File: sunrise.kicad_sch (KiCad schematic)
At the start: 18 parts, among them J1 TOP_HDR, J2 BTM_HDR, U1 LM3410, U2 LP5012

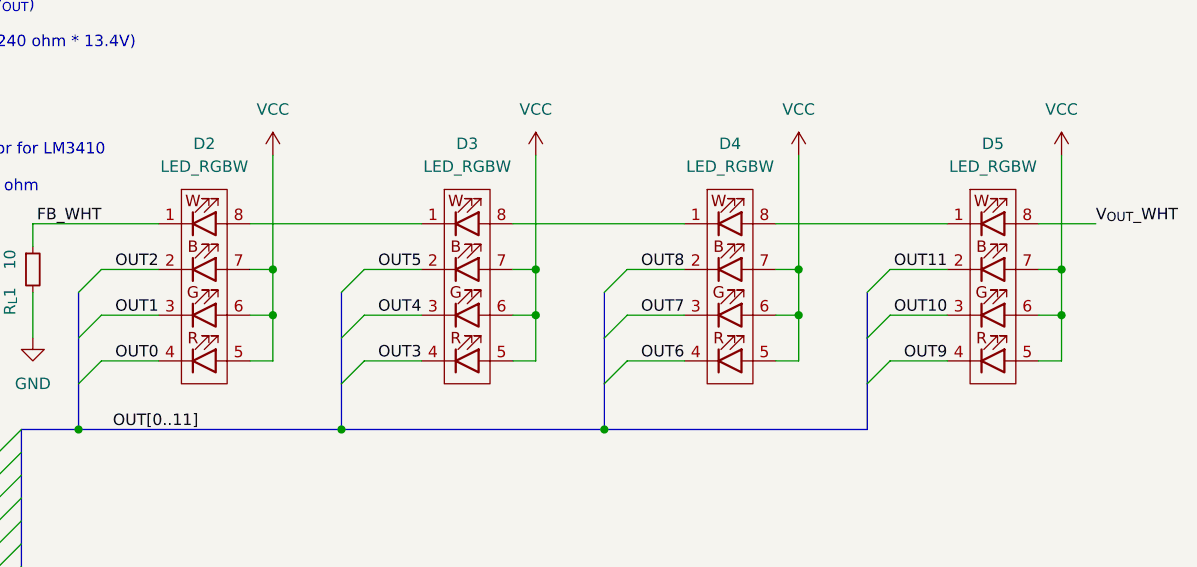
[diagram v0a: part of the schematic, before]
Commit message: Update RGBW footprint and BOM.
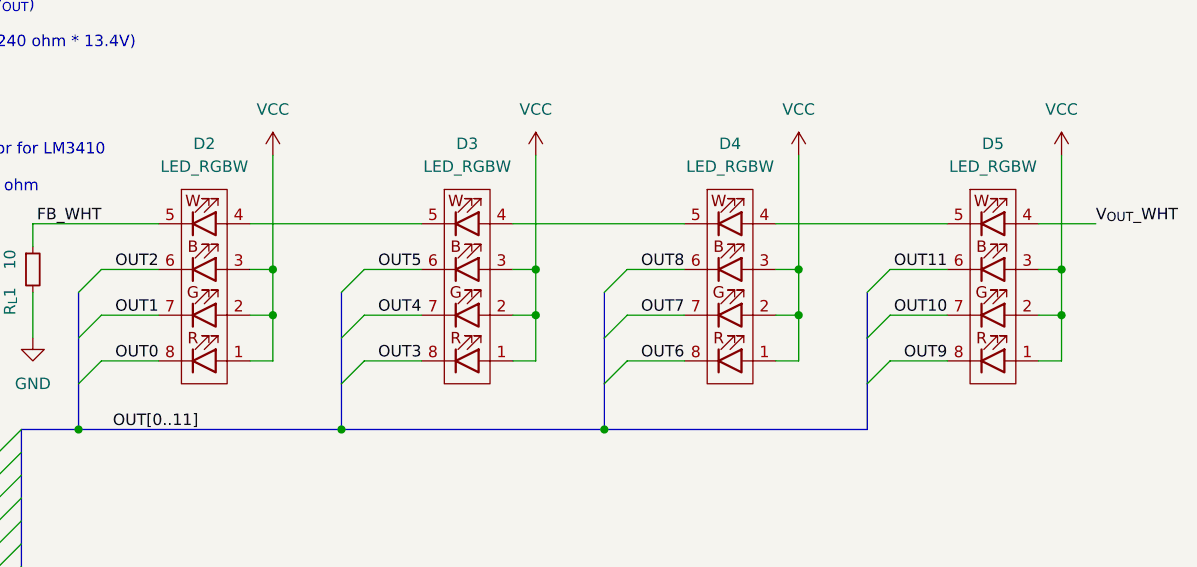
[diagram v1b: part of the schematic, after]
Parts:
- C_{IN}1: Manufacturer (none) -> FH (Guangdong Fenghua Advanced Tech); Manufacturer Part Number (none) -> 0603B105K500NT; Suppier Part Number (none) -> C90540; Supplier (none) -> LCSC
- C_{IN}2: Manufacturer (none) -> Lelon; Manufacturer Part Number (none) -> VE-100M0JTR-0305; Suppier Part Number (none) -> C249448
- C_{OUT}1: Manufacturer (none) -> YAGEO; Manufacturer Part Number (none) -> CC1206FRNPO9BN122; Suppier Part Number (none) -> C541591
- C_{VCAP}1: Manufacturer (none) -> FH (Guangdong Fenghua Advanced Tech); Manufacturer Part Number (none) -> 0603B105K500NT; Suppier Part Number (none) -> C90540
- D1: Manufacturer (none) -> Jiangsu Changjing Electronics Technology Co., Ltd.; Manufacturer Part Number (none) -> B0530WS SE; Suppier Part Number (none) -> C22626
- D2, D3, D4, D5: footprint sunrise:LED_RBGW_PLCC-8 -> sunrise:LED_SMD5050-8; Manufacturer (none) -> TCWIN; Manufacturer Part Number (none) -> TC5050RGBW6D06-4CSAR3-AFW603A; Suppier Part Number (none) -> C784545
- L1: Manufacturer (none) -> TDK; Manufacturer Part Number (none) -> TFM322512ALMA100MTAA; Suppier Part Number (none) -> C2047632
- R1, R2: Manufacturer (none) -> YAGEO; Manufacturer Part Number (none) -> RT0603BRD073K3L; Suppier Part Number (none) -> C309653
- R_{IREF}1: Manufacturer (none) -> PANASONIC; Manufacturer Part Number (none) -> ERJ-6ENF3740V; Suppier Part Number (none) -> C2079472
- R_{L}1: Manufacturer (none) -> YAGEO; Manufacturer Part Number (none) -> RT1206BRE0710RL; Suppier Part Number (none) -> C870973
- U1: Manufacturer (none) -> Texas Instruments; Manufacturer Part Number (none) -> LM3410XMF/NOPB; Suppier Part Number (none) -> C524797
- U2: Manufacturer (none) -> Texas Instruments; Manufacturer Part Number (none) -> LP5012PWR; Suppier Part Number (none) -> C1518705
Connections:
- net FB_WHT: now also D2.5; no longer D2.1
- net OUT0: now also D2.8; no longer D2.4
- net OUT1: now also D2.7; no longer D2.3
- net OUT10: now also D5.7; no longer D5.3
- net OUT11: now also D5.6; no longer D5.2
- net OUT2: now also D2.6; no longer D2.2
- net OUT3: now also D3.8; no longer D3.4
- net OUT4: now also D3.7; no longer D3.3
- net OUT5: now also D3.6; no longer D3.2
- net OUT6: now also D4.8; no longer D4.4
- net OUT7: now also D4.7; no longer D4.3
- net OUT8: now also D4.6; no longer D4.2
- net OUT9: now also D5.8; no longer D5.4
- net VCC: now also D2.1, D2.2, D2.3, D3.1, D3.2, D3.3, D4.1, D4.2, D4.3, D5.1, D5.2, D5.3; no longer D2.5, D2.6, D2.7, D3.5, D3.6, D3.7, D4.5, D4.6, D4.7, D5.5, D5.6, D5.7
- net V_{OUT}_WHT: now also D5.4; no longer D5.8
- new net: D4.4, D5.5
- new net: D3.4, D4.5
- new net: D2.4, D3.5
